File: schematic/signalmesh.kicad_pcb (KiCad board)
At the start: 2 copper layers, 375.2 x 151 mm, 89 parts, among them J1 FPGA I/O, J10 INA219_CONFIG, J11 INA219_CONFIG, J12 AAM_DBG, J13 DSM_DBG, J14 ACM_DBG, J2 FPGA I/O, J3 LCD_display, J4 TDM_DBG, J5 INA219_CONFIG, J6 INA219_CONFIG, J7 INA219_CONFIG, J8 FPGA I/O, J9 FPGA I/O, U1 NUCLEO-H753ZI, U10 INA219AxD, U11 INA219AxD, U12 INA219AxD, U13 INA219AxD, U14 W25Q128JVS, U15 AP2112K-3.3, U16 74HC4050D, U17 NUCLEO-H753ZI, U18 HDSP-7503, U19 HDSP-7503, U2 HDSP-7503, U3 NUCLEO-F303RE, U4 YAAJ_BluePill_Part_Like, U5 24LC256-I_SN, U6 BME280, U7 INA219AxD, U8 24LC256-I_SN, U9 NUCLEO-F446RE

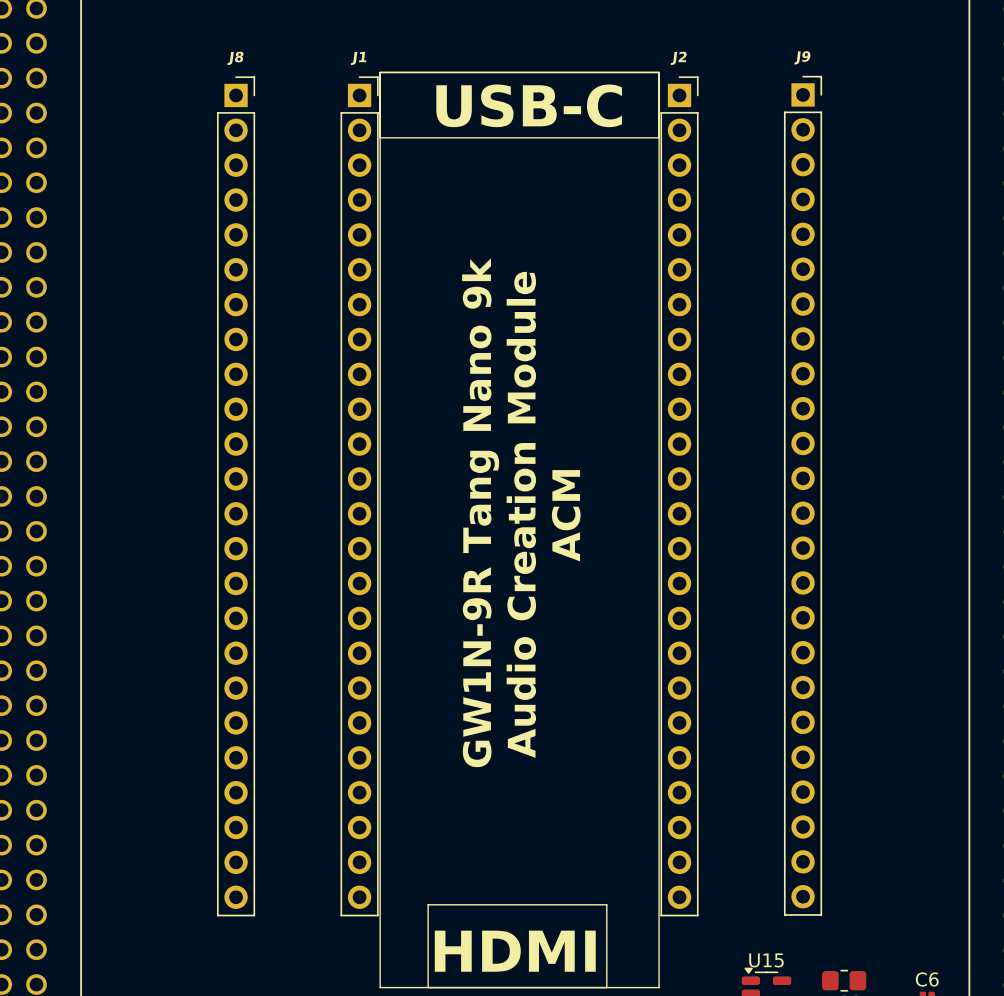
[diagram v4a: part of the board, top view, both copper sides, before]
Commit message: updating FMC pins
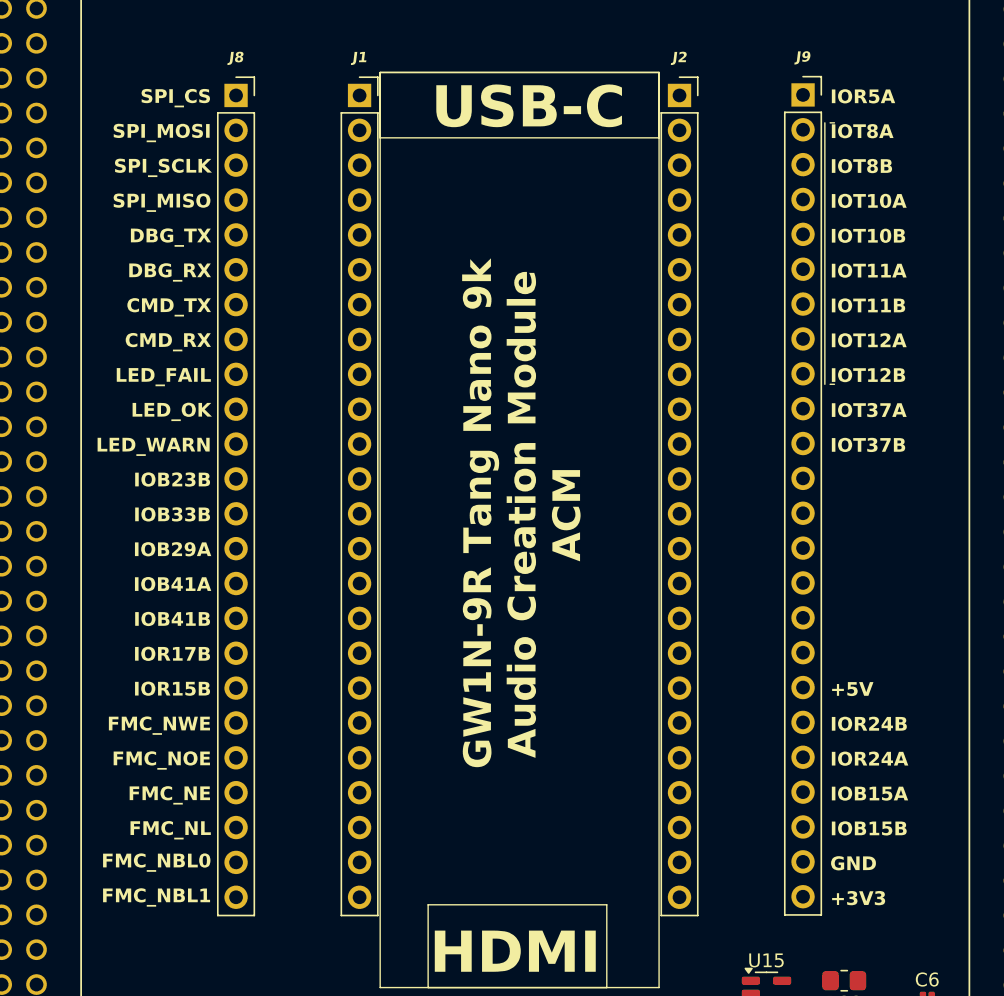
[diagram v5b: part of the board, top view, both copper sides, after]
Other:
- board text added: "+3V3"
- board text added: "+5V"
- board text added: "100nF"
- board text added: "CMD_RX"
- board text added: "CMD_TX"
- board text added: "DBG_RX"
- board text added: "DBG_TX"
- board text added: "FMC_NBL0"
- board text added: "FMC_NBL1"
- board text added: "FMC_NE"
- board text added: "FMC_NL"
- board text added: "FMC_NOE"
- board text added: "FMC_NWE"
- board text added: "IOB15A"
- board text added: "IOB15B"
- board text added: "IOB23B"
- board text added: "IOB29A"
- board text added: "IOB33B"
- board text added: "IOB41A"
- board text added: "IOB41B"
- board text added: "IOR15B"
- board text added: "IOR17B"
- board text added: "IOR24A"
- board text added: "IOR24B"
- board text added: "IOR5A"
- board text added: "IOT10A"
- board text added: "IOT10B"
- board text added: "IOT11A"
- board text added: "IOT11B"
- board text added: "IOT12A"
- board text added: "IOT12B"
- board text added: "IOT37A"
- board text added: "IOT37B"
- board text added: "IOT8A"
- board text added: "IOT8B"
- board text added: "SPI_CS"
- board text added: "SPI_MISO"
- board text added: "SPI_MOSI"
- board text added: "SPI_SCLK"

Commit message: PCB updates
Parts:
- added C10: 0.1uf, Capacitor_SMD:C_0201_0603Metric, F.Cu at (520.4, 195.2)
- added C7: 0.1uf, Capacitor_SMD:C_0201_0603Metric, F.Cu at (548.7, 191.0)
- added C8: 10uf, Capacitor_SMD:C_0201_0603Metric, F.Cu at (216.6, 100.1)
- added C9: 10uf, Capacitor_SMD:C_0201_0603Metric, F.Cu at (216.6, 88.1)
- added D19: LED_PWR, LED_SMD:LED_Kingbright_KPBD-3224, F.Cu at (485.2, 176.6)
- added D20: LED_PWR, LED_SMD:LED_Kingbright_KPBD-3224, F.Cu at (531.8, 188.6)
- added D21: LED_PWR, LED_SMD:LED_Kingbright_KPBD-3224, F.Cu at (493.1, 176.6)
- added D22: LED_OK, LED_SMD:LED_Kingbright_KPBD-3224, F.Cu at (497.0, 176.6)
- added D23: LED_FAIL, LED_SMD:LED_Kingbright_KPBD-3224, F.Cu at (501.0, 176.6)
- added D24: LED_WARN, LED_SMD:LED_Kingbright_KPBD-3224, F.Cu at (504.9, 176.6)
- added D25: LED_PWR, LED_SMD:LED_Kingbright_KPBD-3224, F.Cu at (222.2, 100.4)
- added D26: LED_PWR, LED_SMD:LED_Kingbright_KPBD-3224, F.Cu at (222.2, 89.0)
- added D27: LED_PWR, LED_SMD:LED_Kingbright_KPBD-3224, F.Cu at (516.8, 176.6)
- added J15: INA219_CONFIG, Connector_PinHeader_1.00mm:PinHeader_1x02_P1.00mm_Horizontal, F.Cu at (556.8, 189.9)
- added J16: DSM_DBG, Connector_PinHeader_1.00mm:PinHeader_1x03_P1.00mm_Horizontal, F.Cu at (354.8, 53.8)
- added J17: LCD_display, Connector_PinHeader_1.00mm:PinHeader_1x04_P1.00mm_Horizontal, F.Cu at (509.5, 194.3)
- added R1: 300, Resistor_SMD:R_0805_2012Metric_Pad1.20x1.40mm_HandSolder, F.Cu at (496.9, 181.3)
- added R10: 300, Resistor_SMD:R_0805_2012Metric_Pad1.20x1.40mm_HandSolder, F.Cu at (222.2, 94.4)
- added R2: 300, Resistor_SMD:R_0805_2012Metric_Pad1.20x1.40mm_HandSolder, F.Cu at (537.1, 187.9)
- added R3: 10k, Resistor_SMD:R_0805_2012Metric_Pad1.20x1.40mm_HandSolder, F.Cu at (552.6, 190.8)
- added R4: 10k, Resistor_SMD:R_0805_2012Metric_Pad1.20x1.40mm_HandSolder, F.Cu at (552.6, 187.5)
- added R42: 100, Resistor_SMD:R_0805_2012Metric_Pad1.20x1.40mm_HandSolder, F.Cu at (506.4, 181.3)
- added R43: 300, Resistor_SMD:R_0805_2012Metric_Pad1.20x1.40mm_HandSolder, F.Cu at (506.4, 184.2)
- added R44: 120, Resistor_SMD:R_0805_2012Metric_Pad1.20x1.40mm_HandSolder, F.Cu at (506.4, 187.2)
- added R47: 120, Resistor_SMD:R_0805_2012Metric_Pad1.20x1.40mm_HandSolder, F.Cu at (506.4, 190.1)
- added R5: 300, Resistor_SMD:R_0805_2012Metric_Pad1.20x1.40mm_HandSolder, F.Cu at (496.9, 193.1)
- added R6: 300, Resistor_SMD:R_0805_2012Metric_Pad1.20x1.40mm_HandSolder, F.Cu at (501.7, 181.3)
- added R7: 300, Resistor_SMD:R_0805_2012Metric_Pad1.20x1.40mm_HandSolder, F.Cu at (501.7, 184.2)
- added R8: 300, Resistor_SMD:R_0805_2012Metric_Pad1.20x1.40mm_HandSolder, F.Cu at (501.7, 187.2)
- added R9: 300, Resistor_SMD:R_0805_2012Metric_Pad1.20x1.40mm_HandSolder, F.Cu at (222.2, 105.1)
- added U20: INA219AxD, Package_SO:SOIC-8_3.9x4.9mm_P1.27mm, F.Cu at (543.2, 188.9)
- added U21: 74HC4050D, 74HC4050D:SO16, F.Cu at (209.7, 101.0)
- added U22: AP2112K-3.3, Package_TO_SOT_SMD:SOT-23-5, F.Cu at (216.6, 104.6)
- added U23: W25Q128JVS, Package_SO:SOIC-8_5.3x5.3mm_P1.27mm, F.Cu at (200.6, 99.7)
- added U24: 74HC4050D, 74HC4050D:SO16, F.Cu at (209.8, 90.1)
- added U25: AP2112K-3.3, Package_TO_SOT_SMD:SOT-23-5, F.Cu at (216.6, 93.4)
- added U26: W25Q128JVS, Package_SO:SOIC-8_5.3x5.3mm_P1.27mm, F.Cu at (200.5, 88.8)
- added U27: MCP2551-I-P, Package_DIP:DIP-8_W7.62mm, F.Cu at (484.8, 163.8)
- added U28: 74LVC1G3157, SN74LVC1G3157:SC70-6, F.Cu at (523.1, 190.8)
- added U29: MCP2551-I-P, Package_DIP:DIP-8_W7.62mm, F.Cu at (495.6, 163.8)
- added U30: MCP2551-I-P, Package_DIP:DIP-8_W7.62mm, F.Cu at (506.4, 163.8)
- added U31: MCP2551-I-P, Package_DIP:DIP-8_W7.62mm, F.Cu at (517.1, 163.8)
- moved U2 63.8 mm to (261.3, 54.7)
- moved U18 63.2 mm to (269.9, 54.7)
- moved U4 41.7 mm to (245.6, 56.7), turned to -90 degrees
- moved U19 40.9 mm to (252.5, 54.7)
- moved R11 27.0 mm to (531.2, 144.9), turned to 90 degrees
- moved D1 22.0 mm to (498.4, 144.0)
- moved R15 22.0 mm to (490.4, 156.6)
- moved R16 22.0 mm to (490.4, 144.0)
- moved R17 22.0 mm to (490.4, 148.5)
- moved R18 22.0 mm to (490.4, 152.6)
- moved U5 22.0 mm to (516.6, 154.3)
- moved U8 22.0 mm to (516.6, 146.4)
- moved D2 22.0 mm to (498.3, 148.2)
- moved D3 22.0 mm to (498.3, 152.4)
- moved D4 22.0 mm to (498.3, 156.7)
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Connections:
- J1 pad 10: ACM_LED_FAIL -> ACM_LED_OK
- J1 pad 11: ACM_LED_OK -> ACM_LED_WARN
- J1 pad 12: ACM_LED_WARN -> Net-(J1-Pin_12)
- J1 pad 13: AAM_FMC_CLK -> Net-(J1-Pin_13)
- J1 pad 18: unconnected-(J1-Pin_18-Pad18) -> AAM_FMC_CLK
- J1 pad 9: ACM_LED_PWR -> ACM_LED_FAIL
- J8 pad 10: ACM_LED_FAIL -> ACM_LED_OK
- J8 pad 11: ACM_LED_OK -> ACM_LED_WARN
- J8 pad 12: ACM_LED_WARN -> Net-(J1-Pin_12)
- J8 pad 13: AAM_FMC_CLK -> Net-(J1-Pin_13)
- J8 pad 18: unconnected-(J1-Pin_18-Pad18) -> AAM_FMC_CLK
- J8 pad 9: ACM_LED_PWR -> ACM_LED_FAIL
- U1 pad CN11_18: unconnected-(U1A-5V-PadCN11_18) -> 5V_AAM
- U1 pad CN11_19: Net-(U1A-GND_CN11-PadCN11_19) -> GND
- U1 pad CN11_20: Net-(U1A-GND_CN11-PadCN11_19) -> GND
- U1 pad CN11_22: Net-(U1A-GND_CN11-PadCN11_19) -> GND
- U1 pad CN11_3: unconnected-(U1A-PC12-PadCN11_3) -> AAM_DBG_TX
- U1 pad CN11_32: unconnected-(U1A-PA4-PadCN11_32) -> AAM_DAC_R
- U1 pad CN11_4: unconnected-(U1A-PD2-PadCN11_4) -> AAM_DBG_RX
- U1 pad CN11_47: unconnected-(U1A-PE3-PadCN11_47) -> AAM_INTRPT_RX
- U1 pad CN11_49: Net-(U1A-GND_CN11-PadCN11_19) -> GND
- U1 pad CN11_60: Net-(U1A-GND_CN11-PadCN11_19) -> GND
- U1 pad CN11_62: unconnected-(U1A-PE6-PadCN11_62) -> AAM_INTRPT_TX
- U1 pad CN11_71: Net-(U1A-GND_CN11-PadCN11_19) -> GND
- U1 pad CN11_72: Net-(U1A-GND_CN11-PadCN11_19) -> GND
- U1 pad CN11_8: Net-(U1A-GND_CN11-PadCN11_19) -> GND
- U1 pad CN12_11: unconnected-(U1B-PA5-PadCN12_11) -> AAM_DAC_L
- U17 pad CN11_18: unconnected-(U17A-5V-PadCN11_18) -> 5V_AAM
- U17 pad CN11_19: Net-(U17A-GND_CN11-PadCN11_19) -> GND
- U17 pad CN11_20: Net-(U17A-GND_CN11-PadCN11_19) -> GND
- U17 pad CN11_22: Net-(U17A-GND_CN11-PadCN11_19) -> GND
- U17 pad CN11_3: unconnected-(U17A-PC12-PadCN11_3) -> DSM_DBG_TX
- U17 pad CN11_32: unconnected-(U17A-PA4-PadCN11_32) -> AAM_DAC_R
- U17 pad CN11_4: unconnected-(U17A-PD2-PadCN11_4) -> DSM_DBG_RX
- U17 pad CN11_47: unconnected-(U17A-PE3-PadCN11_47) -> AAM_INTRPT_TX
- U17 pad CN11_49: Net-(U17A-GND_CN11-PadCN11_19) -> GND
- U17 pad CN11_60: Net-(U17A-GND_CN11-PadCN11_19) -> GND
- U17 pad CN11_62: unconnected-(U17A-PE6-PadCN11_62) -> AAM_INTRPT_RX
- U17 pad CN11_71: Net-(U17A-GND_CN11-PadCN11_19) -> GND
- U17 pad CN11_72: Net-(U17A-GND_CN11-PadCN11_19) -> GND
- U17 pad CN11_8: Net-(U17A-GND_CN11-PadCN11_19) -> GND
- U17 pad CN12_11: unconnected-(U17B-PA5-PadCN12_11) -> AAM_DAC_L
- U3 pad CN10_11: unconnected-(U3B-PA5-PadCN10_11) -> UUM_SPI1_SCK
- U3 pad CN10_13: unconnected-(U3B-PA6-PadCN10_13) -> UUM_SPI1_MISO
- U3 pad CN10_15: unconnected-(U3B-PA7-PadCN10_15) -> UUM_SPI1_MOSI
- U3 pad CN10_23: unconnected-(U3B-PA8-PadCN10_23) -> UUM_SPI1_CS
- U3 pad CN10_3: unconnected-(U3B-PB8-PadCN10_3) -> UUM_CAN_RD
- U3 pad CN10_35: unconnected-(U3B-PA2-PadCN10_35) -> UUM_DBG_TX
- U3 pad CN10_37: unconnected-(U3B-PA3-PadCN10_37) -> UUM_DBG_RX
- U3 pad CN10_5: unconnected-(U3B-PB9-PadCN10_5) -> UUM_CAN_TD
- U3 pad CN5_1: (no net) -> unconnected-(U3F-D8-PadCN5_1)
- U3 pad CN5_10: (no net) -> unconnected-(U3F-D15-PadCN5_10)
- U3 pad CN5_2: (no net) -> unconnected-(U3F-D9-PadCN5_2)
- U3 pad CN5_3: (no net) -> unconnected-(U3F-D10-PadCN5_3)
- U3 pad CN5_4: (no net) -> unconnected-(U3F-D11-PadCN5_4)
- U3 pad CN5_5: (no net) -> unconnected-(U3F-D12-PadCN5_5)
- U3 pad CN5_6: (no net) -> unconnected-(U3F-D13-PadCN5_6)
- U3 pad CN5_7: (no net) -> unconnected-(U3F-GND_S6-PadCN5_7)
- U3 pad CN5_8: (no net) -> unconnected-(U3F-AVDD_S6-PadCN5_8)
- U3 pad CN5_9: (no net) -> unconnected-(U3F-D14-PadCN5_9)
- U3 pad CN6_2: (no net) -> unconnected-(U3C-IOREF-PadCN6_2)
- U3 pad CN6_3: (no net) -> unconnected-(U3C-RESET-PadCN6_3)
- U3 pad CN6_4: (no net) -> unconnected-(U3C-+3V3-PadCN6_4)
- U3 pad CN6_5: (no net) -> unconnected-(U3C-+5V-PadCN6_5)
- U3 pad CN6_6: (no net) -> Net-(U3C-GND-PadCN6_6)
- U3 pad CN6_7: (no net) -> Net-(U3C-GND-PadCN6_6)
- U3 pad CN6_8: (no net) -> unconnected-(U3C-VIN-PadCN6_8)
- U3 pad CN7_1: (no net) -> unconnected-(U3A-PC10-PadCN7_1)
- U3 pad CN7_12: (no net) -> unconnected-(U3A-IOREF_S1-PadCN7_12)
- U3 pad CN7_13: (no net) -> unconnected-(U3A-PA13-PadCN7_13)
- U3 pad CN7_14: (no net) -> unconnected-(U3A-RESET_S1-PadCN7_14)
- U3 pad CN7_15: (no net) -> unconnected-(U3A-PA14-PadCN7_15)
- U3 pad CN7_16: (no net) -> 3V3_UUM
- U3 pad CN7_17: (no net) -> unconnected-(U3A-PA15-PadCN7_17)
- U3 pad CN7_18: (no net) -> unconnected-(U3A-+5V_S1-PadCN7_18)
- U3 pad CN7_19: (no net) -> Net-(U3A-GND_S1-PadCN7_19)
- U3 pad CN7_2: (no net) -> unconnected-(U3A-PC11-PadCN7_2)
- U3 pad CN7_20: (no net) -> Net-(U3A-GND_S1-PadCN7_19)
- U3 pad CN7_21: (no net) -> unconnected-(U3A-PB7-PadCN7_21)
- U3 pad CN7_22: (no net) -> Net-(U3A-GND_S1-PadCN7_19)
- U3 pad CN7_23: (no net) -> unconnected-(U3A-PC13-PadCN7_23)
- U3 pad CN7_24: (no net) -> unconnected-(U3A-VIN_S1-PadCN7_24)
- U3 pad CN7_25: (no net) -> UUM_SPI_SEL
- U3 pad CN7_27: (no net) -> unconnected-(U3A-PC15-PadCN7_27)
- U3 pad CN7_28: (no net) -> unconnected-(U3A-PA0-PadCN7_28)
- U3 pad CN7_29: (no net) -> unconnected-(U3A-PF0-PadCN7_29)
- U3 pad CN7_3: (no net) -> unconnected-(U3A-PC12-PadCN7_3)
- U3 pad CN7_30: (no net) -> unconnected-(U3A-PA1-PadCN7_30)
- U3 pad CN7_31: (no net) -> unconnected-(U3A-PF1-PadCN7_31)
- U3 pad CN7_32: (no net) -> unconnected-(U3A-PA4-PadCN7_32)
- U3 pad CN7_33: (no net) -> unconnected-(U3A-VBAT-PadCN7_33)
- U3 pad CN7_34: (no net) -> unconnected-(U3A-PB0-PadCN7_34)
- U3 pad CN7_35: (no net) -> unconnected-(U3A-PC2-PadCN7_35)
- U3 pad CN7_36: (no net) -> unconnected-(U3A-PC1-PadCN7_36)
- U3 pad CN7_37: (no net) -> unconnected-(U3A-PC3-PadCN7_37)
- U3 pad CN7_38: (no net) -> unconnected-(U3A-PC0-PadCN7_38)
- U3 pad CN7_4: (no net) -> unconnected-(U3A-PD2-PadCN7_4)
- U3 pad CN7_5: (no net) -> unconnected-(U3A-VDD-PadCN7_5)
- U3 pad CN7_6: (no net) -> unconnected-(U3A-E5V-PadCN7_6)
- U3 pad CN7_7: (no net) -> unconnected-(U3A-BOOT0-PadCN7_7)
- U3 pad CN7_8: (no net) -> Net-(U3A-GND_S1-PadCN7_19)
- U3 pad CN8_1: (no net) -> unconnected-(U3E-A0-PadCN8_1)
- U3 pad CN8_2: (no net) -> unconnected-(U3E-A1-PadCN8_2)
- U3 pad CN8_3: (no net) -> unconnected-(U3E-A2-PadCN8_3)
- U3 pad CN8_4: (no net) -> unconnected-(U3E-A3-PadCN8_4)
- U3 pad CN8_5: (no net) -> unconnected-(U3E-A4-PadCN8_5)
- U3 pad CN8_6: (no net) -> unconnected-(U3E-A5-PadCN8_6)
- U3 pad CN9_1: (no net) -> unconnected-(U3D-D0-PadCN9_1)
- U3 pad CN9_2: (no net) -> unconnected-(U3D-D1-PadCN9_2)
- U3 pad CN9_3: (no net) -> unconnected-(U3D-D2-PadCN9_3)
- U3 pad CN9_4: (no net) -> unconnected-(U3D-D3-PadCN9_4)
- U3 pad CN9_5: (no net) -> unconnected-(U3D-D4-PadCN9_5)
- U3 pad CN9_6: (no net) -> unconnected-(U3D-D5-PadCN9_6)
- U3 pad CN9_7: (no net) -> unconnected-(U3D-D6-PadCN9_7)
- U3 pad CN9_8: (no net) -> unconnected-(U3D-D7-PadCN9_8)
- U4 pad 6: unconnected-(U4-PA9-Pad6) -> 7SDD_CMD_TX
- U4 pad 7: unconnected-(U4-PA10-Pad7) -> 7SDD_CMD_RX

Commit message: PCB update. CAN routing. making space. may need 4 layers!
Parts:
- moved U28 304.5 mm to (232.0, 101.7)
- moved C10 303.4 mm to (230.5, 105.6)
- moved D27 291.1 mm to (236.4, 98.6), turned to 90 degrees
- moved R42 282.8 mm to (234.0, 105.5)
- moved R43 279.9 mm to (238.0, 104.7), turned to 90 degrees
- moved R1 266.2 mm to (253.1, 74.5)
- moved D19 248.0 mm to (259.9, 72.9)
- moved R5 162.5 mm to (393.0, 68.1), turned to 180 degrees
- moved R8 158.1 mm to (393.0, 72.3), turned to 180 degrees
- moved R7 153.0 mm to (393.0, 76.5), turned to 180 degrees
- moved R6 148.1 mm to (393.0, 80.7), turned to 180 degrees
- moved D24 147.8 mm to (400.4, 72.1), turned to 90 degrees
- moved D21 142.9 mm to (400.5, 67.8), turned to 90 degrees
- moved J17 142.3 mm to (367.3, 198.0), turned to -90 degrees
- moved D23 141.9 mm to (400.5, 76.4), turned to 90 degrees
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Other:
- board text added: "CAN TLM"
- board text added: "UUM_DBG"

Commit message: attempting CAN routing. semi routed pcb
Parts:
- added H1: MountingHole, MountingHole:MountingHole_3.2mm_M3, F.Cu at (189.0, 196.0)
- added H2: MountingHole, MountingHole:MountingHole_3.2mm_M3, F.Cu at (189.0, 55.0)
- added H5: MountingHole, MountingHole:MountingHole_3.2mm_M3, F.Cu at (566.0, 55.0)
- added H6: MountingHole, MountingHole:MountingHole_3.2mm_M3, F.Cu at (566.0, 196.0)
- added J18: LCD_display, Connector_PinHeader_1.00mm:PinHeader_1x04_P1.00mm_Horizontal, F.Cu at (568.9, 66.0)
- moved J17 80.7 mm to (448.0, 199.0)
- moved J3 42.2 mm to (318.5, 199.0)
- moved U19 33.6 mm to (229.5, 79.2)
- moved U2 33.6 mm to (238.3, 79.2)
- moved U18 33.6 mm to (246.9, 79.2)
- moved R1 27.0 mm to (251.1, 101.4)
- moved D19 27.0 mm to (257.9, 99.8)
- moved R47 17.8 mm to (513.3, 180.8)
- moved U31 17.8 mm to (509.5, 192.6)
- moved U17 16.9 mm to (448.1, 122.8)
- moved U1 16.9 mm to (313.4, 122.7)
- moved U30 13.9 mm to (509.7, 174.6)
- moved R44 13.5 mm to (489.0, 180.0), turned to 90 degrees
- moved U6 6.86 mm to (382.0, 190.0)
- moved U4 5.42 mm to (251.0, 56.7)
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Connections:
- net Net-(U27-CANH) renamed /CAN+
- net Net-(U27-CANL) renamed /CAN-
- J1 pad 12: Net-(J1-Pin_12) -> unconnected-(J1-Pin_12-Pad12)
- J1 pad 13: Net-(J1-Pin_13) -> unconnected-(J1-Pin_13-Pad13)
- J8 pad 12: Net-(J1-Pin_12) -> unconnected-(J1-Pin_12-Pad12)
- J8 pad 13: Net-(J1-Pin_13) -> unconnected-(J1-Pin_13-Pad13)
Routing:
- net VDD_UUM: track 0.00 -> 457.7 mm, vias 0 -> 4
- net 5V_7SDD: track 0.00 -> 457.5 mm, vias 0 -> 2
- net TDM_I2C1_SCL: track 0.00 -> 360.0 mm, vias 0 -> 6
- net TDM_I2C1_SDA: track 0.00 -> 359.2 mm, vias 0 -> 7
- net 5V_AAM: track 0.00 -> 330.0 mm, vias 0 -> 2
- net TDM_VDD: track 0.00 -> 324.2 mm, vias 0 -> 4
- net 5V_UUM: track 0.00 -> 299.2 mm, vias 0 -> 2
- net UUM_CAN_RD: track 0.00 -> 279.0 mm, vias 0 -> 1
- net UUM_CAN_TD: track 0.00 -> 275.6 mm, vias 0 -> 1
- net TDM_DBG_RX: track 0.00 -> 218.7 mm, vias 0 -> 1
- net TDM_DBG_TX: track 0.00 -> 207.0 mm, vias 0 -> 1
- net DSM_VDD: track 0.00 -> 182.4 mm, vias 0 -> 2
- net AAM_FMC_D2: track 0.00 -> 172.3 mm, vias 0 -> 1
- net GND: track 0.00 -> 169.3 mm, vias 0 -> 78
- net AAM_FMC_D3: track 0.00 -> 168.2 mm, vias 0 -> 1
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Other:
- board size 375.2 x 151 mm -> 387 x 151 mm
